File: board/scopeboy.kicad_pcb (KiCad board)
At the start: 2 copper layers, 52 x 71.5 mm, 49 parts, among them J1 USB_B_Micro, J2 Conn_02x26_Odd_Even, J3 Conn_02x26_Odd_Even, J4 SM03B-SRSS-TB, SW1 SW_Push, SW2 SW_Push, U1 RP2350_80QFN, U2 NCP1117-3.3_SOT223, U3 W25Q128JVS, U4 DNF, Y1 ABM8-272-T3

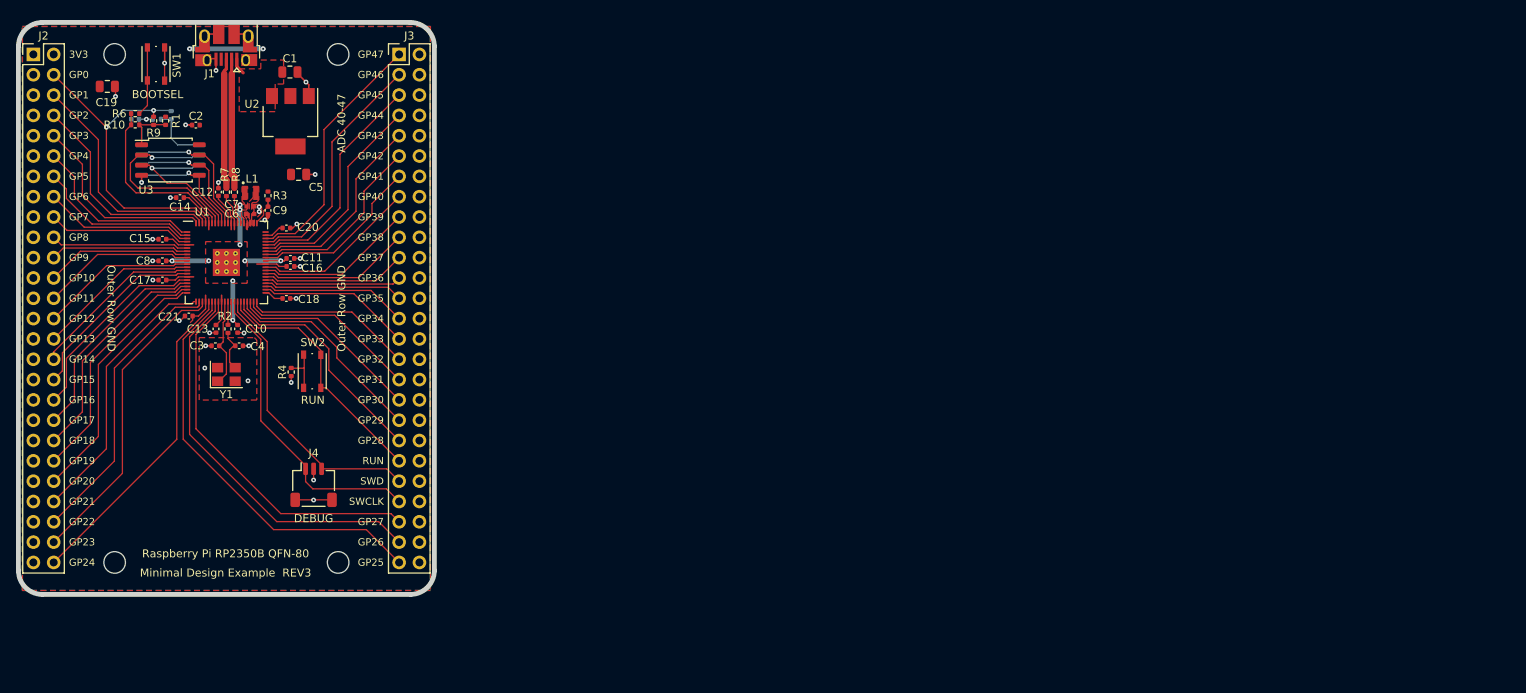
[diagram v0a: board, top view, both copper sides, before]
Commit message: Merged footprints, need to do schematic merge
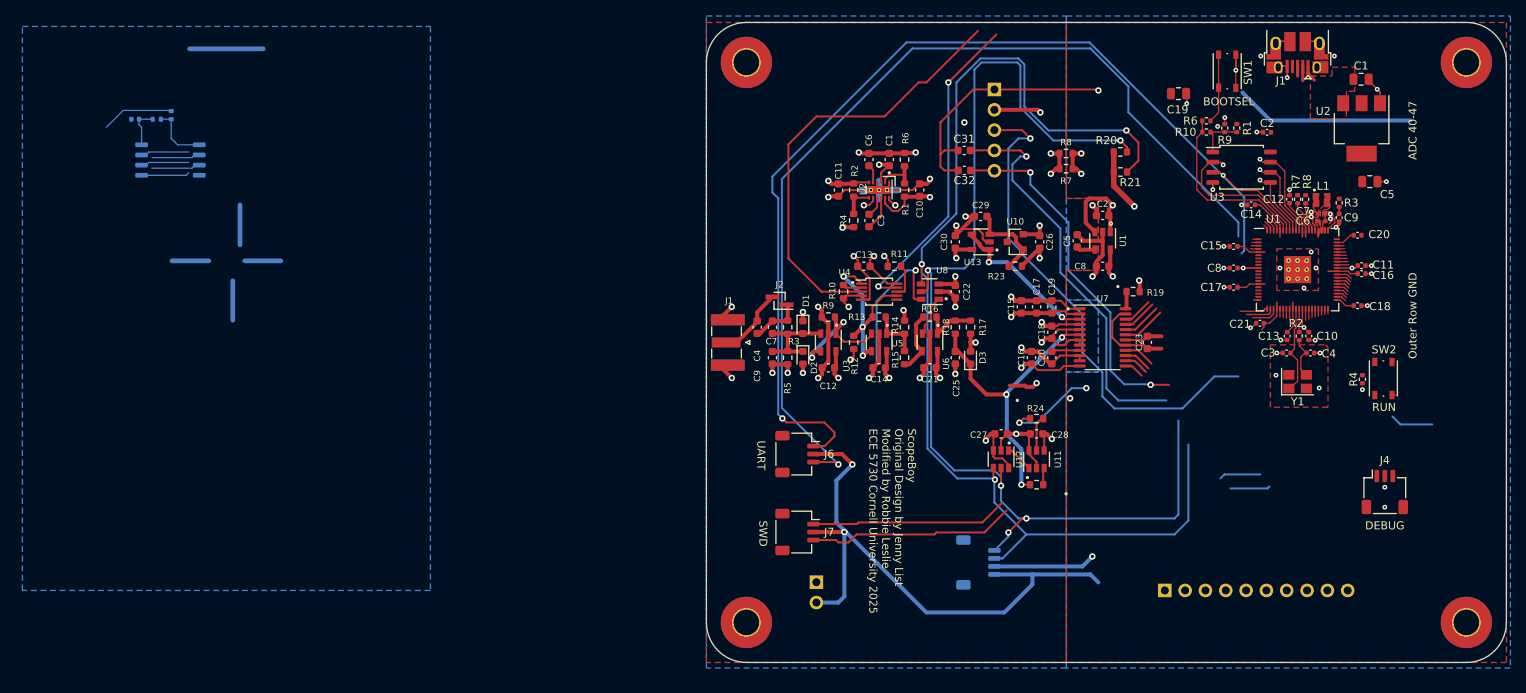
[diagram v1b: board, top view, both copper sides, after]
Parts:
- added C1: 2.2u, Capacitor_SMD:C_0603_1608Metric, F.Cu at (182.9, 87.1)
- added C10: 2.2u, Capacitor_SMD:C_0603_1608Metric, F.Cu at (186.7, 91.0)
- added C11: 2.2u, Capacitor_SMD:C_0603_1608Metric, F.Cu at (176.5, 91.0)
- added C12: 100n, Capacitor_SMD:C_0603_1608Metric, F.Cu at (175.2, 113.2)
- added C13: 100n, Capacitor_SMD:C_0603_1608Metric, F.Cu at (179.7, 100.5)
- added C14: 100n, Capacitor_SMD:C_0603_1608Metric, F.Cu at (181.6, 113.2)
- added C15: 22u, Capacitor_SMD:C_0603_1608Metric, F.Cu at (199.4, 105.6)
- added C16: 100n, Capacitor_SMD:C_0603_1608Metric, F.Cu at (200.6, 111.9)
- added C17: 22u, Capacitor_SMD:C_0603_1608Metric, F.Cu at (201.3, 105.6)
- added C18: 100n, Capacitor_SMD:C_0603_1608Metric, F.Cu at (203.2, 108.7)
- added C19: 100n, Capacitor_SMD:C_0603_1608Metric, F.Cu at (203.2, 105.6)
- added C2: 1u, Capacitor_SMD:C_0603_1608Metric, F.Cu at (209.5, 94.1)
- added C20: 100n, Capacitor_SMD:C_0603_1608Metric, F.Cu at (203.2, 111.9)
- added C21: 100n, Capacitor_SMD:C_0603_1608Metric, F.Cu at (187.9, 113.2)
- added C22: 100n, Capacitor_SMD:C_0603_1608Metric, F.Cu at (191.1, 103.7)
- added C23: 100n, Capacitor_SMD:C_0603_1608Metric, F.Cu at (215.1, 110.0)
- added C25: 160p, Capacitor_SMD:C_0603_1608Metric, F.Cu at (191.1, 111.9)
- added C26: 1u, Capacitor_SMD:C_0603_1608Metric, F.Cu at (201.7, 97.4)
- added C27: 100n, Capacitor_SMD:C_0603_1608Metric, F.Cu at (196.8, 121.4)
- added C28: 100n, Capacitor_SMD:C_0603_1608Metric, F.Cu at (201.3, 121.4)
- added C29: 100n, Capacitor_SMD:C_0603_1608Metric, F.Cu at (194.3, 94.3)
- added C3: 2.2u, Capacitor_SMD:C_0603_1608Metric, F.Cu at (180.3, 94.8)
- added C30: 100n, Capacitor_SMD:C_0603_1608Metric, F.Cu at (191.1, 97.4)
- added C31: 10nF, Capacitor_SMD:C_0603_1608Metric, F.Cu at (192.2, 86.0)
- added C32: 10nF, Capacitor_SMD:C_0603_1608Metric, F.Cu at (192.2, 88.5)
- added C4: 10n, Capacitor_SMD:C_0603_1608Metric, F.Cu at (166.3, 108.1)
- added C5: 10n, Capacitor_SMD:C_0603_1608Metric, F.Cu at (206.4, 97.3)
- added C6: 4.7u, Capacitor_SMD:C_0603_1608Metric, F.Cu at (180.3, 87.1)
- added C7: 1p, Capacitor_SMD:C_0603_1608Metric, F.Cu at (168.3, 108.1)
- added C8: 2.2u, Capacitor_SMD:C_0603_1608Metric, F.Cu at (209.5, 100.5)
- added C9: 6.8p, Capacitor_SMD:C_0603_1608Metric, F.Cu at (168.3, 111.9)
- added D1: D, Diode_SMD:D_0603_1608Metric, F.Cu at (172.1, 108.1)
- added D2: D, Diode_SMD:D_0603_1608Metric, F.Cu at (172.1, 111.9)
- added D3: D, Diode_SMD:D_0603_1608Metric, F.Cu at (193.0, 111.9)
- added J1: Conn_01x02, Connector_Coaxial:SMA_Samtec_SMA-J-P-X-ST-EM1_EdgeMount, F.Cu at (162.7, 110.0)
- added J4: Conn_01x10, Connector_PinHeader_2.54mm:PinHeader_1x10_P2.54mm_Vertical, B.Cu at (217.3, 141.0)
- added J5: SM04B-SRSS-TB, Connector_JST:JST_SH_SM04B-SRSS-TB_1x04-1MP_P1.00mm_Horizontal, B.Cu at (194.0, 137.5)
- added J6: SM03B-SRSS-TB, Connector_JST:JST_SH_SM03B-SRSS-TB_1x03-1MP_P1.00mm_Horizontal, F.Cu at (171.4, 124.0)
- added J7: SM03B-SRSS-TB, Connector_JST:JST_SH_SM03B-SRSS-TB_1x03-1MP_P1.00mm_Horizontal, F.Cu at (171.4, 133.7)
- added J8: Conn_01x02, Connector_PinHeader_2.54mm:PinHeader_1x02_P2.54mm_Vertical, B.Cu at (173.8, 140.0)
- added R1: 87k, Resistor_SMD:R_0603_1608Metric, F.Cu at (184.8, 91.0)
- added R10: 47, Resistor_SMD:R_0603_1608Metric, F.Cu at (177.1, 103.7)
- added R11: 100, Resistor_SMD:R_0603_1608Metric, F.Cu at (183.5, 100.5)
- added R12: 100, Resistor_SMD:R_0603_1608Metric, F.Cu at (178.4, 110.0)
- added R13: 680, Resistor_SMD:R_0603_1608Metric, F.Cu at (181.6, 106.8)
- added R14: 1k, Resistor_SMD:R_0603_1608Metric, F.Cu at (184.8, 108.1)
- added R15: 100, Resistor_SMD:R_0603_1608Metric, F.Cu at (184.8, 111.9)
- added R16: 100, Resistor_SMD:R_0603_1608Metric, F.Cu at (187.9, 106.8)
- added R17: 1k, Resistor_SMD:R_0603_1608Metric, F.Cu at (193.0, 108.1)
- added R18: 100, Resistor_SMD:R_0603_1608Metric, F.Cu at (191.1, 108.1)
- added R19: 22, Resistor_SMD:R_0603_1608Metric, F.Cu at (213.3, 103.7)
- added R2: 87k, Resistor_SMD:R_0603_1608Metric, F.Cu at (178.4, 91.0)
- added R20: 4.7k, Resistor_SMD:R_0603_1608Metric, F.Cu at (211.8, 86.2)
- added R21: 4.7k, Resistor_SMD:R_0603_1608Metric, F.Cu at (211.8, 88.7)
- added R22: 1MEG, Resistor_SMD:R_0603_1608Metric, F.Cu at (201.3, 127.8)
- added R23: 1k, Resistor_SMD:R_0603_1608Metric, F.Cu at (198.6, 100.5)
- added R24: 22, Resistor_SMD:R_0603_1608Metric, F.Cu at (201.3, 119.5)
- added R3: 680k, Resistor_SMD:R_0603_1608Metric, F.Cu at (170.2, 108.1)
- added R4: 50k, Resistor_SMD:R_0603_1608Metric, F.Cu at (178.4, 94.8)
- added R5: 100k, Resistor_SMD:R_0603_1608Metric, F.Cu at (170.2, 111.9)
- added R6: 50k, Resistor_SMD:R_0603_1608Metric, F.Cu at (184.8, 87.1)
- added R7: 0, Resistor_SMD:R_0603_1608Metric, F.Cu at (205.0, 88.3)
- added R8: 0, Resistor_SMD:R_0603_1608Metric, F.Cu at (205.0, 86.4)
- added R9: 1k, Resistor_SMD:R_0603_1608Metric, F.Cu at (175.2, 106.8)
- added U1: LP2985-3.3, Package_TO_SOT_SMD:SOT-23-5, F.Cu at (209.5, 97.3)
- added U10: LM4040DBZ-2.0, Package_TO_SOT_SMD:SOT-23, F.Cu at (198.6, 97.4)
- added U11: TLV3501, Package_TO_SOT_SMD:SOT-23-6, F.Cu at (201.3, 124.6)
- added U12: DAC5571, Package_TO_SOT_SMD:SOT-23-6, F.Cu at (196.8, 124.6)
- added U13: TLV271, Package_TO_SOT_SMD:SOT-23-5, F.Cu at (194.3, 97.4)
- added U2: LM27762, Package_SON:WSON-12-1EP_3x2mm_P0.5mm_EP1x2.65_ThermalVias, F.Cu at (181.6, 91.0)
- added U3: OPA354, Package_TO_SOT_SMD:SOT-23-5, F.Cu at (175.2, 110.0)
- added U4: ADG621, Package_SO:MSOP-10_3x3mm_P0.5mm, F.Cu at (181.6, 103.7)
- added U5: LMH6629, Package_TO_SOT_SMD:SOT-23-5, F.Cu at (181.6, 110.0)
- added U6: OPA830, Package_TO_SOT_SMD:SOT-23-5, F.Cu at (187.9, 110.0)
- added U7: ADC08100, Package_SO:TSSOP-24_4.4x7.8mm_P0.65mm, F.Cu at (209.5, 109.4)
- added U8: DAC5571, Package_TO_SOT_SMD:SOT-23-6, F.Cu at (187.9, 103.7)
- H1, H2, H3, H4: footprint MountingHole:MountingHole_2.7mm_M2.5 -> MountingHole:MountingHole_3.2mm_M3_Pad_TopBottom
- J2: value Conn_02x26_Odd_Even -> Conn_01x02_Male; footprint Connector_PinHeader_2.54mm:PinHeader_2x26_P2.54mm_Vertical -> Connector_PinHeader_1.00mm:PinHeader_1x02_P1.00mm_Vertical_SMD_Pin1Left
- J3: value Conn_02x26_Odd_Even -> Conn_01x05; footprint Connector_PinHeader_2.54mm:PinHeader_2x26_P2.54mm_Vertical -> Connector_PinHeader_2.54mm:PinHeader_1x05_P2.54mm_Vertical; moved to B.Cu
- moved H2 157.9 mm to (255.0, 145.0)
- moved H3 154.3 mm to (255.0, 75.0)
- moved C1 133.9 mm to (241.8, 77.1)
- moved C10 133.9 mm to (235.3, 109.2)
- moved C11 133.9 mm to (241.9, 100.4)
- moved C12 133.9 mm to (232.9, 92.1)
- moved C15 133.9 mm to (225.9, 98.0)
- moved C16 133.9 mm to (241.9, 101.4)
- moved C17 133.9 mm to (225.9, 103.1)
- moved C18 133.9 mm to (241.4, 105.4)
- moved C2 133.9 mm to (230.1, 83.7)
- moved C20 133.9 mm to (241.4, 96.6)
- moved C3 133.9 mm to (232.5, 111.3)
- moved C4 133.9 mm to (235.5, 111.3)
- moved C5 133.9 mm to (242.9, 89.9)
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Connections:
- J2 pad 1: GND -> Net-(J2-Pin_1)
- J2 pad 2: +3V3 -> Net-(J1-Pin_1)
- J3 pad 1: /GPIO47_ADC7 -> GND
- J3 pad 2: GND -> +3V3Pico
- J3 pad 3: /GPIO46_ADC6 -> ROTSW
- J3 pad 4: GND -> ROTDT
- J3 pad 5: /GPIO45_ADC5 -> ROTCLK
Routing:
- net GNDA: track 0.00 -> 365.9 mm, vias 0 -> 26
- net GND: track 38.8 -> 355.5 mm, vias 29 -> 36
- net +3.3VA: track 0.00 -> 204.0 mm, vias 0 -> 14
- net +3V3Pico: track 0.00 -> 156.3 mm, vias 0 -> 2
- net SCL: track 0.00 -> 141.9 mm, vias 0 -> 3
- net VSYS: track 0.00 -> 141.5 mm, vias 0 -> 4
- net SDA: track 0.00 -> 141.3 mm, vias 0 -> 5
- net -3V3: track 0.00 -> 134.7 mm, vias 0 -> 9
- net RX: track 0.00 -> 122.7 mm, vias 0 -> 1
- net TX: track 0.00 -> 118.3 mm, vias 0 -> 1
- net TRIG: track 0.00 -> 72.8 mm, vias 0 -> 2
- net ROTSW: track 0.00 -> 63.3 mm, vias 0 -> 1
- net SEL1: track 0.00 -> 54.7 mm
- net /GPIO25: track 52.1 -> 1.10 mm
- net ROTDT: track 0.00 -> 50.4 mm, vias 0 -> 1
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- added copper zone on In2.Cu, net +3V3
- added copper zone on In2.Cu, net -3V3
- added copper zone on In1.Cu, net GND
- added copper zone on B.Cu, net GNDA
- added copper zone on F.Cu, net GNDA
- added copper zone on In1.Cu, net GNDA
- added copper zone on In2.Cu, net VSYS
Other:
- board size 52 x 71.5 mm -> 100 x 80 mm
- copper layers 2 -> 4
- board text added: "Battery Charger"
- board text added: "Joystick"
- board text added: "Rotary"
- board text added: "ScopeBoy Original Design by Jenny List Modified by Robbie Leslie ECE 5730 Cornell University 2025"
- board text added: "TFT"
- board text added: "UART"
- board text removed: "3V3"
- board text removed: "GP0"
- board text removed: "GP1"
- board text removed: "GP10"
- board text removed: "GP11"
- board text removed: "GP12"
- board text removed: "GP13"
- board text removed: "GP14"
- board text removed: "GP15"
- board text removed: "GP16"
- board text removed: "GP17"
- board text removed: "GP18"
- board text removed: "GP19"
- board text removed: "GP2"
- board text removed: "GP20"
- board text removed: "GP21"
- board text removed: "GP22"
- board text removed: "GP23"
- board text removed: "GP24"
- board text removed: "GP25"
- board text removed: "GP26"
- board text removed: "GP27"
- board text removed: "GP28"
- board text removed: "GP29"
- board text removed: "GP3"
- board text removed: "GP30"
- board text removed: "GP31"
- board text removed: "GP32"
- board text removed: "GP33"
- board text removed: "GP34"
- board text removed: "GP35"
- board text removed: "GP36"
- board text removed: "GP37"
- board text removed: "GP38"
- board text removed: "GP39"
- board text removed: "GP4"
- board text removed: "GP40"
- board text removed: "GP41"
- board text removed: "GP42"
- board text removed: "GP43"
- board text removed: "GP44"
- board text removed: "GP45"
- board text removed: "GP46"
- board text removed: "GP47"
- board text removed: "GP5"
- board text removed: "GP6"
- board text removed: "GP7"
- board text removed: "GP8"
- board text removed: "GP9"
- board text removed: "Minimal Design Example REV3"
- board text removed: "Raspberry Pi RP2350B QFN-80"
- board text removed: "SWCLK"

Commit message: Re-moved with back side
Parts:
- moved C22 135.1 mm to (223.7, 81.5)
- moved R11 135.1 mm to (228.2, 81.0)
- moved R13 135.1 mm to (226.4, 81.5)
- moved U4 135.1 mm to (228.1, 86.6)
- moved C13 1.92 mm to (233.8, 107.7)
- moved C14 1.92 mm to (229.3, 91.3)
- moved C19 1.92 mm to (220.2, 77.4)
- moved C21 1.92 mm to (230.4, 106.1)
- moved C9 1.92 mm to (240.3, 92.9)
- moved R2 1.92 mm to (235.3, 107.7)
- moved R3 1.92 mm to (240.3, 91.0)
- moved SW1 1.92 mm to (226.3, 74.6)
- moved C1 1.92 mm to (243.0, 75.6)
- moved C10 1.92 mm to (236.5, 107.7)
- moved C11 1.92 mm to (243.1, 98.9)
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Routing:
- net SDA: track 141.3 -> 110.4 mm
- net SCL: track 141.9 -> 111.4 mm
- net (no net): track 0.00 -> 22.4 mm
- net +3V3Pico: track 156.3 -> 133.8 mm
- net ROTSW: track 63.3 -> 54.7 mm
- net SCK: track 5.41 -> 0.00 mm
- net SWCLK: track 30.0 -> 24.7 mm
- net SWIO: track 30.9 -> 25.9 mm
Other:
- board text removed: "ADC 40-47"
- board text removed: "Outer Row GND"
